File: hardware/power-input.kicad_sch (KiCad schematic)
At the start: 29 parts

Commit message: Very minor schematic tweaks
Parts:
- U?: value TCP01-M12 -> TCPP01-M12
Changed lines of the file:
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@@
 			)
 		)
-		(property "Value" "TCP01-M12"
+		(property "Value" "TCPP01-M12"
 			(at 139.3033 113.03 0)
 			(show_name no)

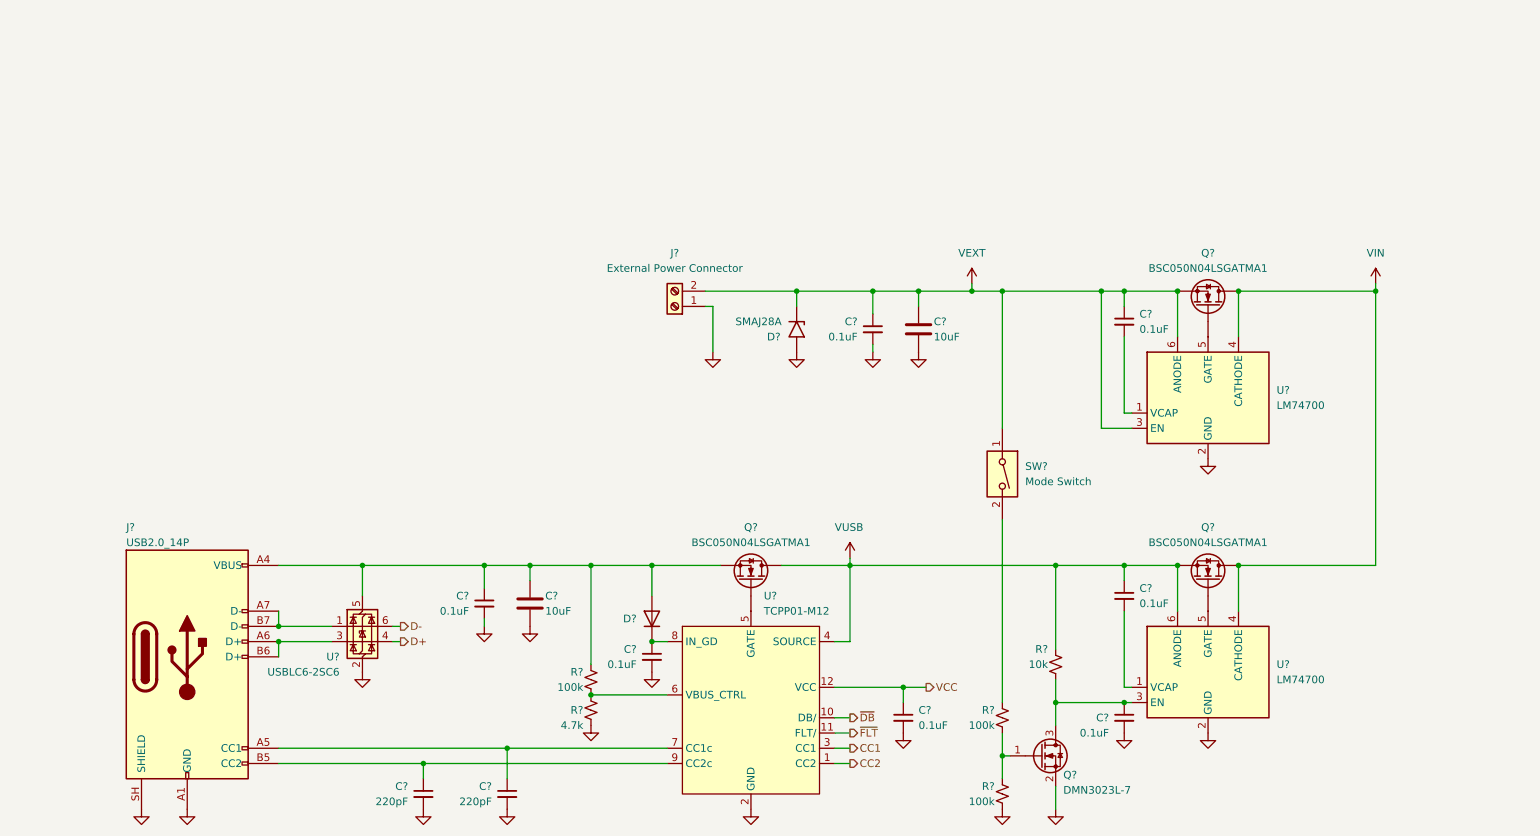
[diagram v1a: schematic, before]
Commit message: Remove USB C PD and refine power input
Deleted USB C PD features due to complexity. Simplified power input schematic. Sourced PSU, connectors, crimps, and created external harness schematics.
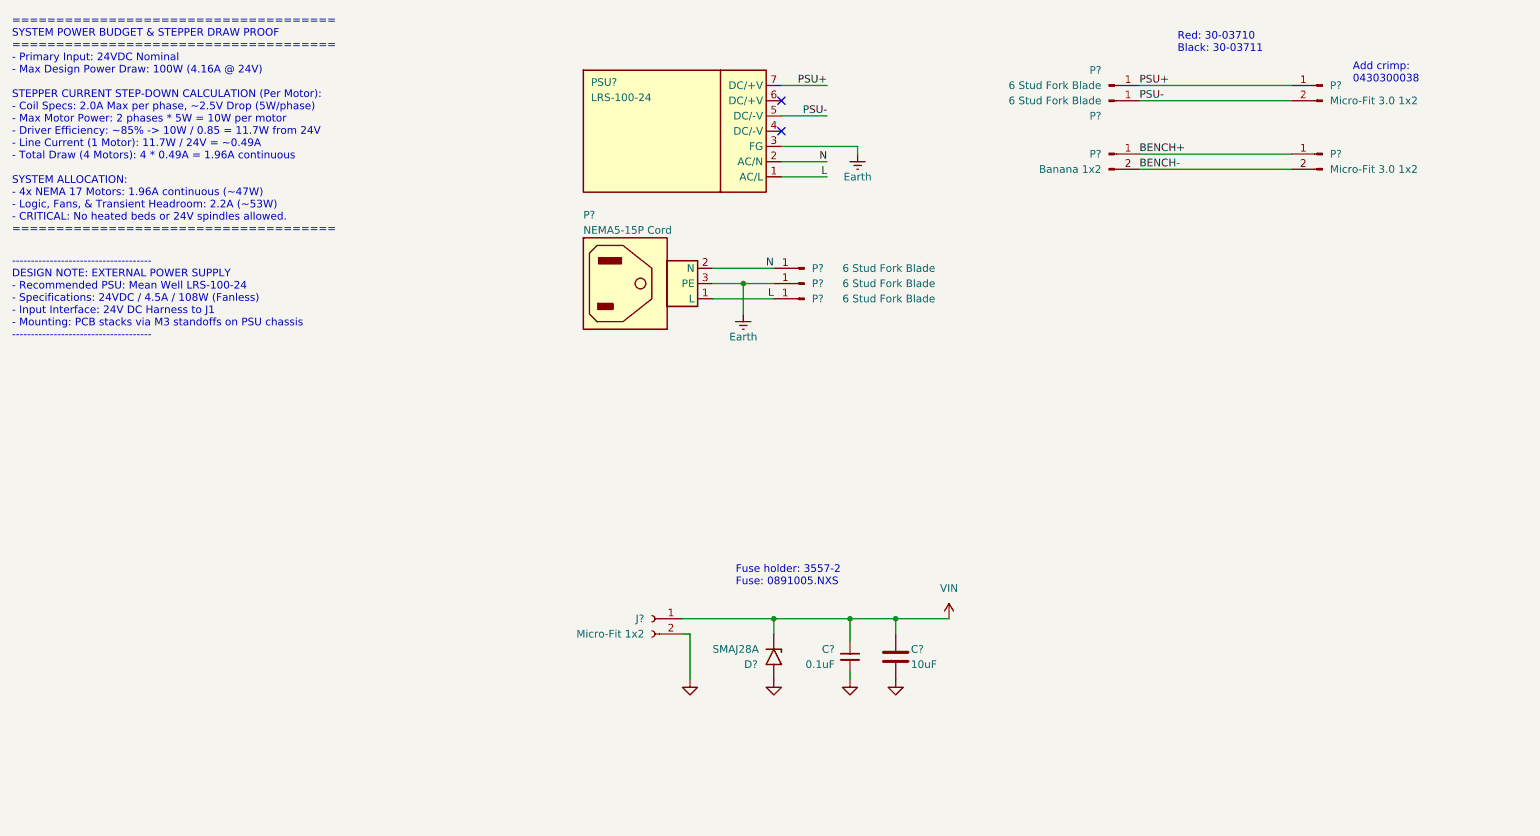
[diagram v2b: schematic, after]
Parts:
- removed C? (x6): 0.1uF, Capacitor_SMD:C_0603_1608Metric_Pad1.08x0.95mm_HandSolder, symbol Device:C_Small
- removed C? (x2): 220pF, Capacitor_SMD:C_0603_1608Metric_Pad1.08x0.95mm_HandSolder, symbol Device:C_Small
- removed C?: 10uF, Capacitor_SMD:C_1210_3225Metric_Pad1.33x2.70mm_HandSolder, symbol Device:C
- removed D?: RB751V-40, Diode_SMD:D_SOD-323_HandSoldering, symbol Device:D
- removed J?: External Power Connector, TerminalBlock_CUI:TerminalBlock_CUI_TB007-508-02_1x02_P5.08mm_Horizontal, symbol Connector:Screw_Terminal_01x02
- removed J?: USB2.0_14P, symbol Connector:USB_C_Receptacle_USB2.0_14P
- removed Q? (x3): BSC050N04LSGATMA1, Package_SON:Infineon_PG-TDSON-8_6.15x5.15mm, symbol stepping-stone:BSC050N04LSGATMA1
- removed Q?: DMN3023L-7, Package_TO_SOT_SMD:SOT-23, symbol stepping-stone:DMN3023L-7
- removed R?: 10k, symbol Device:R_Small_US
- removed R? (x3): 100k, Resistor_SMD:R_0603_1608Metric_Pad0.98x0.95mm_HandSolder, symbol Device:R_Small_US
- removed R?: 4.7k, symbol Device:R_Small_US
- removed SW?: Mode Switch, Button_Switch_SMD:SW_DIP_SPSTx01_Slide_9.78x4.72mm_W8.61mm_P2.54mm, symbol Switch:SW_DIP_x01
- removed U? (x2): LM74700, Package_TO_SOT_SMD:SOT-23-6, symbol Power_Management:LM74700
- removed U?: USBLC6-2SC6, Package_TO_SOT_SMD:SOT-23-6, symbol Power_Protection:USBLC6-2SC6
- removed U?: TCPP01-M12, Package_DFN_QFN:QFN-12-1EP_3x3mm_P0.5mm_EP1.45x1.45mm, symbol stepping-stone:TCPP01-M12
- added J?: Micro-Fit 1x2, symbol Connector:Conn_01x02_Socket
- added P? (x2): Micro-Fit 3.0 1x2, symbol Connector:Conn_01x02_Pin
- added P? (x5): 6 Stud Fork Blade, symbol Connector:Conn_01x01_Pin
- added P?: Banana 1x2, symbol Connector:Conn_01x02_Pin
- added P?: NEMA5-15P Cord, symbol stepping-stone:NEMA5-15P Cord
- added PSU?: LRS-100-24, symbol stepping-stone:LRS-100-24
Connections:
- net VEXT is gone; now on net VIN: C?.1, C?.1, D?.1 (A1)
- net GND: now also J?.2 (Pin_2)
- net VIN: now also J?.1 (Pin_1)
- new net BENCH+: P?.1 (Pin_1), P?.1 (Pin_1)
- new net BENCH-: P?.2 (Pin_2), P?.2 (Pin_2)
- new net Earth: P?.1 (Pin_1), P?.3 (PE), PSU?.3 (FG)
- new net L: P?.1 (L), P?.1 (Pin_1), PSU?.1 (AC/L)
- new net N: P?.1 (Pin_1), P?.2 (N), PSU?.2 (AC/N)
- new net PSU+: P?.1 (Pin_1), P?.1 (Pin_1), PSU?.7 (DC/+V)
- new net PSU-: P?.1 (Pin_1), P?.2 (Pin_2), PSU?.5 (DC/-V)
- no-connect marks 0 -> 2
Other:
- note added: "------------------------------------- DESIGN NOTE: EXTERNAL POWER SUPPLY - Recommended PSU: Mean Well LRS-100-24 - Specifications: 24VDC / 4.5A / 108W (Fanless) - Input Interface: 24V DC Harness to J1 - Mounting: PCB stacks via M3 standoffs on PSU chassis -------------------------------------"
- note added: "===================================== SYSTEM POWER BUDGET & STEPPER DRAW PROOF ===================================== - Primary Input: 24VDC Nominal - Max Design Power Draw: 100W (4.16A @ 24V) STEPPER CURRENT STEP-DOWN CALCULATION (Per Motor): - Coil Specs: 2.0A Max per phase, ~2.5V Drop (5W/phase) - Max Motor Power: 2 phases * 5W = 10W per motor - Driver Efficiency: ~85% -> 10W / 0.85 = 11.7W fro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"
- note added: "Add crimp: 0430300038"
- note added: "Fuse holder: 3557-2 Fuse: 0891005.NXS"
- note added: "Red: 30-03710 Black: 30-03711"
- moved on the sheet: C?, D?

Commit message: Improve connector symbols
Created custom symbols for connectors, and added symbols for crimps and wires for BOM purposes.
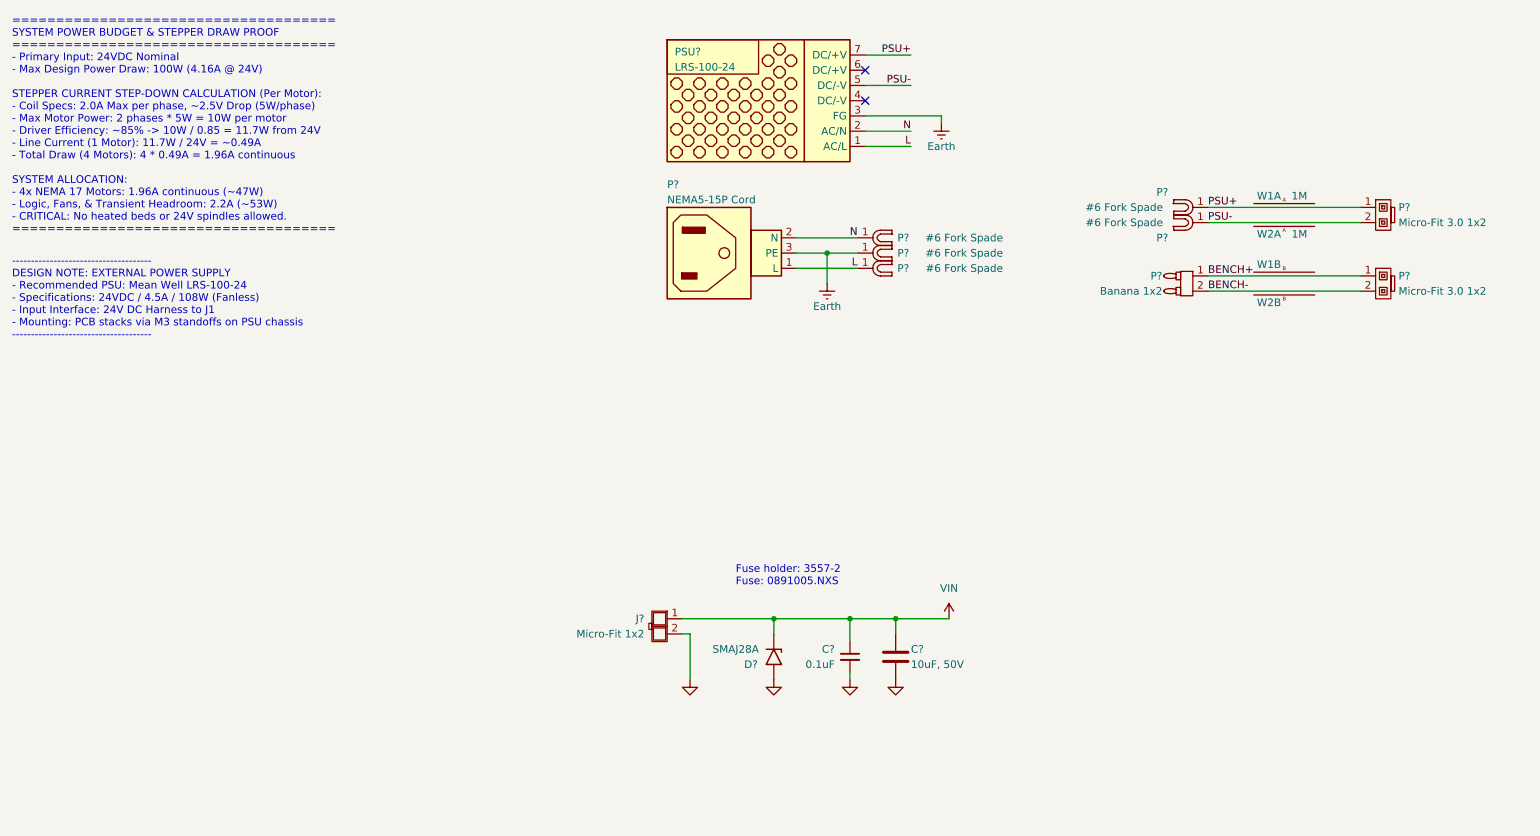
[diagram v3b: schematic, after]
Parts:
- removed J?: Micro-Fit 1x2, symbol Connector:Conn_01x02_Socket
- removed P? (x2): Micro-Fit 3.0 1x2, symbol Connector:Conn_01x02_Pin
- removed P? (x5): 6 Stud Fork Blade, symbol Connector:Conn_01x01_Pin
- removed P?: Banana 1x2, symbol Connector:Conn_01x02_Pin
- added J?: Micro-Fit 1x2, symbol stepping-stone:Micro-Fit 3.0 1x2 Jack
- added P?: Banana 1x2, symbol stepping-stone:2-Pin Banana Plug
- added P? (x5): #6 Fork Spade, symbol stepping-stone:#6 Fork Spade
- added P? (x2): Micro-Fit 3.0 1x2, symbol stepping-stone:Micro-Fit_3.0_1x2 Plug
- added W1, W2, W3, W4: 18 AWG Crimp, symbol stepping-stone:Micro-Fit 3.0 18AWG Crimp
- added W1: 1M, symbol stepping-stone:18AWG Stranded Red Wire
- added W2: 1M, symbol stepping-stone:18AWG Stranded Black Wire
- C?: value 10uF -> 10uF, 50V
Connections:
- net BENCH+: now also P?.1, P?.1
- net BENCH-: now also P?.2, P?.2
- net Earth: now also P?.1
- net GND: now also J?.2
- net L: now also P?.1
- net N: now also P?.1
- net PSU+: now also P?.1, P?.1
- net PSU-: now also P?.1, P?.2
- net VIN: now also J?.1
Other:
- note removed: "Add crimp: 0430300038"
- note removed: "Red: 30-03710 Black: 30-03711"
- moved on the sheet: P?

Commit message: Add fuses
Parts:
- added F1: 30A 500V, symbol stepping-stone:3557-2
- added F2, F3, F4: 5A, symbol stepping-stone:0891005.NXS
- gave numbers to parts that had none: 10
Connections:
- net VIN: now also F1.3, F1.4; no longer C?.1, C?.1, D?.1 (A1), J1.1
- new net: C?.1, C?.1, D?.1 (A1), F1.1, F1.2, J1.1
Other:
- note removed: "Fuse holder: 3557-2 Fuse: 0891005.NXS"
- title: Power Input & Source Select -> Power Input
